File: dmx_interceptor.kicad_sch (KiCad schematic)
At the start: 8 parts, among them J1 TB010-508-02BE, J2 TB010-508-02BE, J3 TB004-508-03BE, J4 TB004-508-03BE, U1 ARDUINO_PRO_MINI

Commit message: output files for ordering & pcb fix
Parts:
- J1, J2: footprint CUI_TB010-508-02BE -> dmx_interceptor:CUI_TB010-508-02BE; MPN (none) -> TB010-508-02BE
- J3, J4: footprint CUI_TB004-508-03BE -> dmx_interceptor:CUI_TB004-508-03BE; MPN (none) -> TB004-508-03BE
- R1: footprint mart_library:smd_0603_1608-Metric -> dmx_interceptor:smd_0603_1608-Metric
- U1: footprint MODULE_ARDUINO_PRO_MINI -> dmx_interceptor:MODULE_ARDUINO_PRO_MINI; MPN (none) -> DEV-11113
- mod1, mod2: footprint mart_library:max485_to_rs485 -> dmx_interceptor:max485_to_rs485
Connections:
- net 5V: now also U1.JP1_4 (VCC)
- net D_RX: now also U1.JP7_11 (RXI_2)
- net D_TX: now also U1.JP7_12 (TXO_2)
- net GND: now also U1.JP7_9 (GND_2)
- net RE_DE_RX: now also U1.JP7_4 (D6)
- net RE_DE_TX: now also U1.JP7_5 (D5)
- net VIN: now also U1.JP6_1 (RAW)
- net switch: now also U1.JP7_1 (D9)
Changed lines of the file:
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@@
 (kicad_sch (version 20230121) (generator eeschema)
   (paper "A4")
+  (junction (at 143.51 66.04) (diameter 0) (color 0 0 0 0)
+  )
   (junction (at 200.66 73.66) (diameter 0) (color 0 0 0 0)
   )
+  (junction (at 158.75 119.38) (diameter 0) (color 0 0 0 0)
+  )
   (junction (at 212.09 66.04) (diameter 0) (color 0 0 0 0)
   )
-  (junction (at 158.75 119.38) (diameter 0) (color 0 0 0 0)
-  )
-  (junction (at 143.51 29.21) (diameter 0) (color 0 0 0 0)
+  (junction (at 158.75 121.92) (diameter 0) (color 0 0 0 0)
   )
   (junction (at 167.64 46.99) (diameter 0) (color 0 0 0 0)
@@
   (junction (at 200.66 104.14) (diameter 0) (color 0 0 0 0)
   )
-  (junction (at 143.51 119.38) (diameter 0) (color 0 0 0 0)
-  )
   (junction (at 165.1 71.12) (diameter 0) (color 0 0 0 0)
   )
@@
   (junction (at 200.66 57.15) (diameter 0) (color 0 0 0 0)
   )
-  (junction (at 158.75 121.92) (diameter 0) (color 0 0 0 0)
-  )
   (wire (pts (xy 153.67 91.44) (xy 153.67 54.61))
     (stroke (width 0) (type default))
@@
     (stroke (width 0) (type default))
   )
+  (wire (pts (xy 143.51 29.21) (xy 143.51 66.04))
+    (stroke (width 0) (type default))
+  )
   (wire (pts (xy 212.09 66.04) (xy 195.58 66.04))
     (stroke (width 0) (type default))
@@
     (stroke (width 0) (type default))
   )
-  (wire (pts (xy 142.24 91.44) (xy 153.67 91.44))
-    (stroke (width 0) (type default))
-  )
   (wire (pts (xy 200.66 109.22) (xy 200.66 104.14))
     (stroke (width 0) (type default))
@@
     (stroke (width 0) (type default))
   )
-  (wire (pts (xy 143.51 119.38) (xy 142.24 119.38))
+  (wire (pts (xy 143.51 121.92) (xy 158.75 121.92))
+    (stroke (width 0) (type default))
+  )
+  (wire (pts (xy 143.51 91.44) (xy 153.67 91.44))
     (stroke (width 0) (type default))
   )
@@
     (stroke (width 0) (type default))
   )
-  (wire (pts (xy 143.51 29.21) (xy 143.51 68.58))
+  (wire (pts (xy 143.51 66.04) (xy 143.51 68.58))
     (stroke (width 0) (type default))
   )
@@
     (stroke (width 0) (type default))
   )
-  (wire (pts (xy 212.09 29.21) (xy 143.51 29.21))
+  (wire (pts (xy 143.51 101.6) (xy 156.21 101.6))
+    (stroke (width 0) (type default))
+  )
+  (wire (pts (xy 143.51 116.84) (xy 158.75 116.84))
     (stroke (width 0) (type default))
   )
@@
     (stroke (width 0) (type default))
   )
-  (wire (pts (xy 142.24 71.12) (xy 144.78 71.12))
-    (stroke (width 0) (type default))
-  )
   (wire (pts (xy 125.73 153.67) (xy 212.09 153.67))
     (stroke (width 0) (type default))
@@
     (stroke (width 0) (type default))
   )
-  (wire (pts (xy 142.24 104.14) (xy 165.1 104.14))
+  (wire (pts (xy 143.51 29.21) (xy 212.09 29.21))
+    (stroke (width 0) (type default))
+  )
+  (wire (pts (xy 158.75 116.84) (xy 158.75 119.38))
+    (stroke (width 0) (type default))
+  )
+  (wire (pts (xy 143.51 111.76) (xy 146.05 111.76))
     (stroke (width 0) (type default))
   )
@@
     (stroke (width 0) (type default))
   )
+  (wire (pts (xy 143.51 104.14) (xy 165.1 104.14))
+    (stroke (width 0) (type default))
+  )
   (wire (pts (xy 92.71 127) (xy 146.05 127))
     (stroke (width 0) (type default))
   )
-  (wire (pts (xy 142.24 88.9) (xy 147.32 88.9))
+  (wire (pts (xy 143.51 119.38) (xy 158.75 119.38))
     (stroke (width 0) (type default))
   )
@@
     (stroke (width 0) (type default))
   )
-  (wire (pts (xy 143.51 29.21) (xy 142.24 29.21))
+  (wire (pts (xy 143.51 88.9) (xy 147.32 88.9))
     (stroke (width 0) (type default))
   )
@@
     (stroke (width 0) (type default))
   )
-  (wire (pts (xy 142.24 121.92) (xy 158.75 121.92))
-    (stroke (width 0) (type default))
-  )
   (wire (pts (xy 153.67 54.61) (xy 163.83 54.61))
     (stroke (width 0) (type default))
@@
     (stroke (width 0) (type default))
   )
-  (wire (pts (xy 158.75 119.38) (xy 143.51 119.38))
-    (stroke (width 0) (type default))
-  )
-  (wire (pts (xy 142.24 101.6) (xy 156.21 101.6))
-    (stroke (width 0) (type default))
-  )
   (wire (pts (xy 165.1 71.12) (xy 172.72 71.12))
     (stroke (width 0) (type default))
   )
+  (wire (pts (xy 143.51 71.12) (xy 144.78 71.12))
+    (stroke (width 0) (type default))
+  )
   (wire (pts (xy 195.58 44.45) (xy 212.09 44.45))
     (stroke (width 0) (type default))
@@
     (stroke (width 0) (type default))
   )
-  (wire (pts (xy 158.75 121.92) (xy 158.75 119.38))
+  (wire (pts (xy 158.75 119.38) (xy 158.75 121.92))
     (stroke (width 0) (type default))
   )
@@
     (stroke (width 0) (type default))
   )
+  (wire (pts (xy 200.66 104.14) (xy 176.53 104.14))
+    (stroke (width 0) (type default))
+  )
+  (wire (pts (xy 212.09 44.45) (xy 212.09 29.21))
+    (stroke (width 0) (type default))
+  )
+  (wire (pts (xy 200.66 57.15) (xy 200.66 73.66))
+    (stroke (width 0) (type default))
+  )
+  (wire (pts (xy 66.04 109.22) (xy 53.34 109.22))
+    (stroke (width 0) (type default))
+  )
+  (wire (pts (xy 218.44 49.53) (xy 218.44 54.61))
+    (stroke (width 0) (type default))
+  )
+  (wire (pts (xy 172.72 68.58) (xy 165.1 68.58))
+    (stroke (width 0) (type default))
+  )
+  (wire (pts (xy 158.75 132.08) (xy 86.36 132.08))
+    (stroke (width 0) (type default))
+  )
+  (wire (pts (xy 156.21 46.99) (xy 156.21 101.6))
+    (stroke (width 0) (type default))
+  )
   (wire (pts (xy 158.75 121.92) (xy 158.75 132.08))
     (stroke (width 0) (type default))
   )
-  (wire (pts (xy 200.66 104.14) (xy 176.53 104.14))
-    (stroke (width 0) (type default))
-  )
-  (wire (pts (xy 143.51 116.84) (xy 143.51 119.38))
-    (stroke (width 0) (type default))
-  )
-  (wire (pts (xy 212.09 44.45) (xy 212.09 29.21))
-    (stroke (width 0) (type default))
-  )
-  (wire (pts (xy 200.66 57.15) (xy 200.66 73.66))
-    (stroke (width 0) (type default))
-  )
-  (wire (pts (xy 66.04 109.22) (xy 53.34 109.22))
-    (stroke (width 0) (type default))
-  )
-  (wire (pts (xy 218.44 49.53) (xy 218.44 54.61))
-    (stroke (width 0) (type default))
-  )
-  (wire (pts (xy 172.72 68.58) (xy 165.1 68.58))
-    (stroke (width 0) (type default))
-  )
-  (wire (pts (xy 158.75 132.08) (xy 86.36 132.08))
-    (stroke (width 0) (type default))
-  )
-  (wire (pts (xy 156.21 46.99) (xy 156.21 101.6))
-    (stroke (width 0) (type default))
-  )
   (wire (pts (xy 77.47 33.02) (xy 144.78 33.02))
     (stroke (width 0) (type default))
   )
   (wire (pts (xy 200.66 73.66) (xy 195.58 73.66))
-    (stroke (width 0) (type default))
-  )
-  (wire (pts (xy 142.24 111.76) (xy 146.05 111.76))
     (stroke (width 0) (type default))
   )
@@
       (effects (font (size 1.27 1.27)) (justify left))
     )
-    (property "Footprint" "CUI_TB004-508-03BE" (at 242.57 54.61 0)
+    (property "Footprint" "dmx_interceptor:CUI_TB004-508-03BE" (at 242.57 54.61 0)
       (effects (font (size 1.27 1.27)) (justify left bottom) hide)
     )
@@
     )
     (property "mpn" "TB004-508-03BE" (at 248.92 39.37 0)
+      (effects (font (size 1.27 1.27)) hide)
+    )
+    (property "MPN" "TB004-508-03BE" (at 242.57 54.61 0)
       (effects (font (size 1.27 1.27)) hide)
     )
@@
       (effects (font (size 1.27 1.27)) (justify left))
     )
-    (property "Footprint" "CUI_TB004-508-03BE" (at 242.57 76.2 0)
+    (property "Footprint" "dmx_interceptor:CUI_TB004-508-03BE" (at 242.57 76.2 0)
       (effects (font (size 1.27 1.27)) (justify left bottom) hide)
     )
@@
     )
     (property "mpn" "TB004-508-03BE" (at 248.92 60.96 0)
+      (effects (font (size 1.27 1.27)) hide)
+    )
+    (property "MPN" "TB004-508-03BE" (at 242.57 76.2 0)
       (effects (font (size 1.27 1.27)) hide)
     )
@@
       (effects (font (size 1.27 1.27)))
     )
-    (property "Footprint" "CUI_TB010-508-02BE" (at 115.57 153.67 0)
+    (property "Footprint" "dmx_interceptor:CUI_TB010-508-02BE" (at 115.57 153.67 0)
       (effects (font (size 1.27 1.27)) (justify left bottom) hide)
     )
@@
     )
     (property "mnp" "TB010-508-02BE" (at 115.57 153.67 0)
+      (effects (font (size 1.27 1.27)) hide)
+    )
+    (property "MPN" "TB010-508-02BE" (at 115.57 153.67 0)
       (effects (font (size 1.27 1.27)) hide)
     )
@@
       (effects (font (size 1.27 1.27)) hide)
     )
-    (property "Footprint" "mart_library:smd_0603_1608-Metric" (at 69.85 103.632 90)
+    (property "Footprint" "dmx_interceptor:smd_0603_1608-Metric" (at 69.85 103.632 90)
       (effects (font (size 1.27 1.27)) hide)
     )
@@
       (effects (font (size 1.27 1.27)))
     )
-    (property "Footprint" "mart_library:max485_to_rs485" (at 181.61 63.5 0)
+    (property "Footprint" "dmx_interceptor:max485_to_rs485" (at 181.61 63.5 0)
       (effects (font (size 1.27 1.27)) hide)
     )
@@
       (effects (font (size 1.27 1.27)))
     )
-    (property "Footprint" "mart_library:max485_to_rs485" (at 181.61 85.09 0)
+    (property "Footprint" "dmx_interceptor:max485_to_rs485" (at 181.61 85.09 0)
       (effects (font (size 1.27 1.27)) hide)
     )
@@
       (effects (font (size 1.27 1.27)))
     )
-    (property "Footprint" "CUI_TB010-508-02BE" (at 67.31 33.02 0)
+    (property "Footprint" "dmx_interceptor:CUI_TB010-508-02BE" (at 67.31 33.02 0)
       (effects (font (size 1.27 1.27)) (justify left bottom) hide)
     )
@@
     )
     (property "mnp" "TB010-508-02BE" (at 67.31 33.02 0)
+      (effects (font (size 1.27 1.27)) hide)
+    )
+    (property "MPN" "TB010-508-02BE" (at 67.31 33.02 0)
       (effects (font (size 1.27 1.27)) hide)
     )
@@
       (effects (font (size 1.27 1.27)))
     )
-    (property "Footprint" "MODULE_ARDUINO_PRO_MINI" (at 125.73 93.98 0)
+    (property "Footprint" "dmx_interceptor:MODULE_ARDUINO_PRO_MINI" (at 125.73 93.98 0)
       (effects (font (size 1.27 1.27)) (justify left bottom) hide)
     )
@@
       (effects (font (size 1.27 1.27)) hide)
     )
+    (property "MPN" "DEV-11113" (at 125.73 93.98 0)
+      (effects (font (size 1.27 1.27)) hide)
+    )

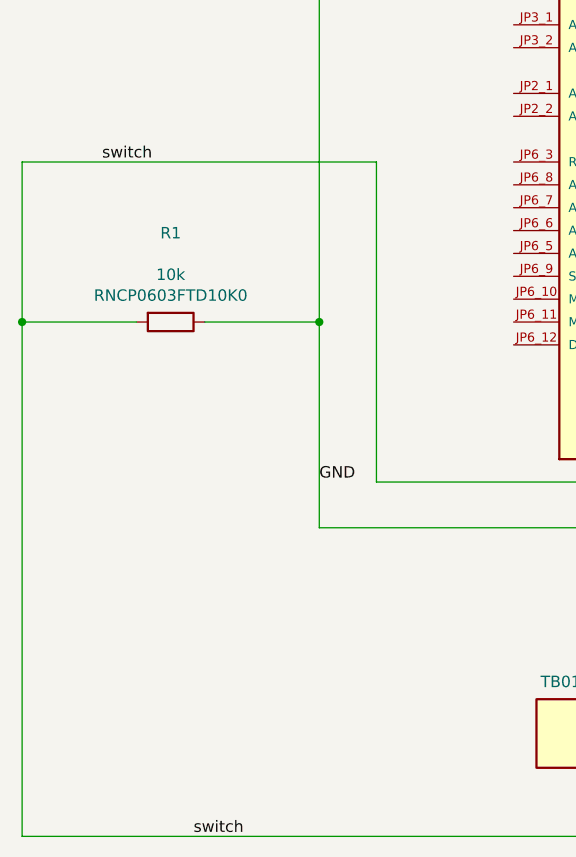
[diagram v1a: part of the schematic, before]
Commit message: change resistor to throughole
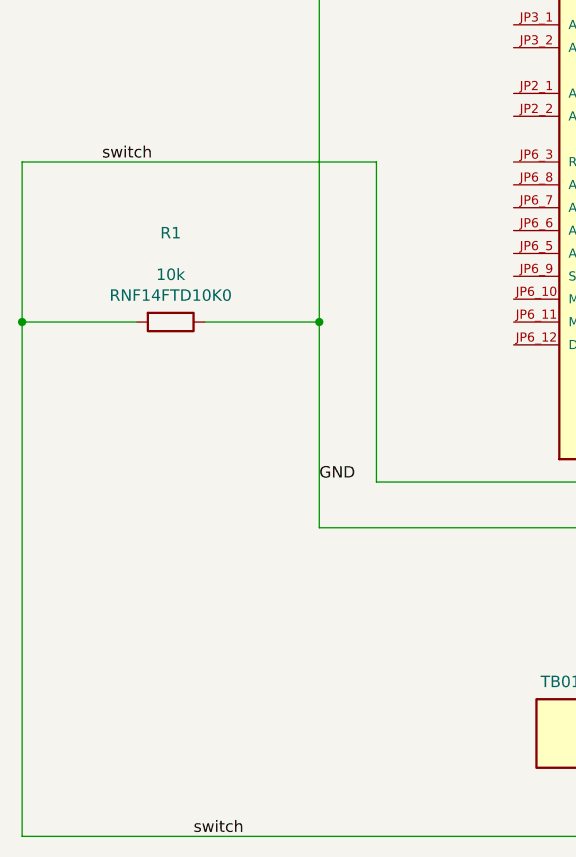
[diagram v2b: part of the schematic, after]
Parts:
- R1: footprint dmx_interceptor:smd_0603_1608-Metric -> dmx_interceptor:R_THT; MPN RNCP0603FTD10K0 -> RNF14FTD10K0
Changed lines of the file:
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@@
   (junction (at 212.09 66.04) (diameter 0) (color 0 0 0 0)
   )
+  (junction (at 86.36 109.22) (diameter 0) (color 0 0 0 0)
+  )
+  (junction (at 53.34 109.22) (diameter 0) (color 0 0 0 0)
+  )
   (junction (at 158.75 121.92) (diameter 0) (color 0 0 0 0)
   )
@@
   (junction (at 200.66 78.74) (diameter 0) (color 0 0 0 0)
   )
-  (junction (at 53.34 109.22) (diameter 0) (color 0 0 0 0)
-  )
   (junction (at 200.66 104.14) (diameter 0) (color 0 0 0 0)
   )
@@
   (junction (at 212.09 44.45) (diameter 0) (color 0 0 0 0)
   )
-  (junction (at 86.36 109.22) (diameter 0) (color 0 0 0 0)
-  )
   (junction (at 200.66 57.15) (diameter 0) (color 0 0 0 0)
   )
@@
     (stroke (width 0) (type default))
   )
+  (wire (pts (xy 86.36 109.22) (xy 86.36 132.08))
+    (stroke (width 0) (type default))
+  )
   (wire (pts (xy 92.71 91.44) (xy 92.71 127))
     (stroke (width 0) (type default))
@@
     (stroke (width 0) (type default))
   )
-  (wire (pts (xy 53.34 109.22) (xy 53.34 91.44))
+  (wire (pts (xy 53.34 91.44) (xy 53.34 109.22))
     (stroke (width 0) (type default))
   )
@@
     (stroke (width 0) (type default))
   )
+  (wire (pts (xy 53.34 109.22) (xy 53.34 166.37))
+    (stroke (width 0) (type default))
+  )
   (wire (pts (xy 53.34 91.44) (xy 92.71 91.44))
     (stroke (width 0) (type default))
@@
     (stroke (width 0) (type default))
   )
+  (wire (pts (xy 163.83 54.61) (xy 163.83 66.04))
+    (stroke (width 0) (type default))
+  )
+  (wire (pts (xy 143.51 88.9) (xy 147.32 88.9))
+    (stroke (width 0) (type default))
+  )
+  (wire (pts (xy 167.64 49.53) (xy 167.64 46.99))
+    (stroke (width 0) (type default))
+  )
+  (wire (pts (xy 165.1 71.12) (xy 165.1 104.14))
+    (stroke (width 0) (type default))
+  )
+  (wire (pts (xy 153.67 54.61) (xy 163.83 54.61))
+    (stroke (width 0) (type default))
+  )
+  (wire (pts (xy 200.66 52.07) (xy 200.66 57.15))
+    (stroke (width 0) (type default))
+  )
+  (wire (pts (xy 224.79 73.66) (xy 232.41 73.66))
+    (stroke (width 0) (type default))
+  )
+  (wire (pts (xy 53.34 109.22) (xy 66.04 109.22))
+    (stroke (width 0) (type default))
+  )
+  (wire (pts (xy 165.1 71.12) (xy 172.72 71.12))
+    (stroke (width 0) (type default))
+  )
+  (wire (pts (xy 143.51 71.12) (xy 144.78 71.12))
+    (stroke (width 0) (type default))
+  )
+  (wire (pts (xy 195.58 44.45) (xy 212.09 44.45))
+    (stroke (width 0) (type default))
+  )
+  (wire (pts (xy 195.58 71.12) (xy 218.44 71.12))
+    (stroke (width 0) (type default))
+  )
+  (wire (pts (xy 158.75 119.38) (xy 158.75 121.92))
+    (stroke (width 0) (type default))
+  )
+  (wire (pts (xy 200.66 104.14) (xy 200.66 78.74))
+    (stroke (width 0) (type default))
+  )
   (wire (pts (xy 73.66 109.22) (xy 86.36 109.22))
     (stroke (width 0) (type default))
   )
-  (wire (pts (xy 163.83 54.61) (xy 163.83 66.04))
-    (stroke (width 0) (type default))
-  )
-  (wire (pts (xy 143.51 88.9) (xy 147.32 88.9))
-    (stroke (width 0) (type default))
-  )
-  (wire (pts (xy 167.64 49.53) (xy 167.64 46.99))
-    (stroke (width 0) (type default))
-  )
-  (wire (pts (xy 165.1 71.12) (xy 165.1 104.14))
-    (stroke (width 0) (type default))
-  )
-  (wire (pts (xy 153.67 54.61) (xy 163.83 54.61))
-    (stroke (width 0) (type default))
-  )
-  (wire (pts (xy 200.66 52.07) (xy 200.66 57.15))
-    (stroke (width 0) (type default))
-  )
-  (wire (pts (xy 224.79 73.66) (xy 232.41 73.66))
-    (stroke (width 0) (type default))
-  )
-  (wire (pts (xy 165.1 71.12) (xy 172.72 71.12))
-    (stroke (width 0) (type default))
-  )
-  (wire (pts (xy 143.51 71.12) (xy 144.78 71.12))
-    (stroke (width 0) (type default))
-  )
-  (wire (pts (xy 195.58 44.45) (xy 212.09 44.45))
-    (stroke (width 0) (type default))
-  )
-  (wire (pts (xy 195.58 71.12) (xy 218.44 71.12))
-    (stroke (width 0) (type default))
-  )
-  (wire (pts (xy 158.75 119.38) (xy 158.75 121.92))
-    (stroke (width 0) (type default))
-  )
-  (wire (pts (xy 200.66 104.14) (xy 200.66 78.74))
-    (stroke (width 0) (type default))
-  )
   (wire (pts (xy 212.09 44.45) (xy 212.09 66.04))
     (stroke (width 0) (type default))
@@
     (stroke (width 0) (type default))
   )
-  (wire (pts (xy 66.04 109.22) (xy 53.34 109.22))
-    (stroke (width 0) (type default))
-  )
   (wire (pts (xy 218.44 49.53) (xy 218.44 54.61))
     (stroke (width 0) (type default))
@@
   )
   (wire (pts (xy 167.64 46.99) (xy 172.72 46.99))
-    (stroke (width 0) (type default))
-  )
-  (wire (pts (xy 53.34 166.37) (xy 53.34 109.22))
-    (stroke (width 0) (type default))
-  )
-  (wire (pts (xy 86.36 132.08) (xy 86.36 109.22))
     (stroke (width 0) (type default))
   )
@@
       (effects (font (size 1.27 1.27)) hide)
     )
-    (property "Footprint" "dmx_interceptor:smd_0603_1608-Metric" (at 69.85 103.632 90)
+    (property "Footprint" "dmx_interceptor:R_THT" (at 69.85 103.632 90)
       (effects (font (size 1.27 1.27)) hide)
     )
@@
       (effects (font (size 1.27 1.27)) hide)
     )
-    (property "MPN" "RNCP0603FTD10K0" (at 69.85 106.2736 90)
+    (property "MPN" "RNF14FTD10K0" (at 69.85 106.2736 90)
       (effects (font (size 1.27 1.27)))
     )
